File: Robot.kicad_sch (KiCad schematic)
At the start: 5 parts, among them J1 XT60 4Port PDB, J2 LM2596 Buck Converter, J3 WAGO 221 - 5 Port

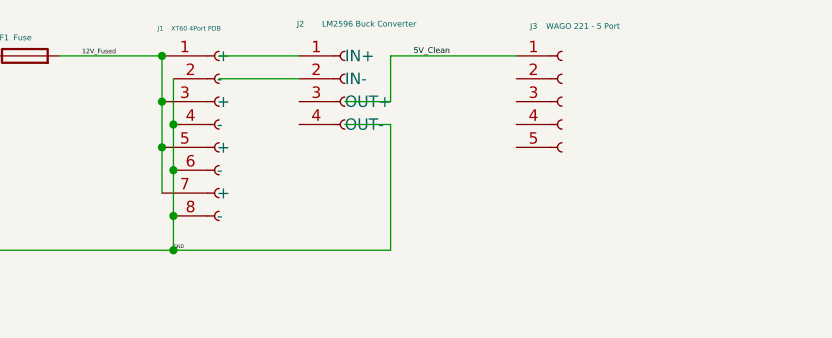
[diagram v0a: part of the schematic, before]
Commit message: fix some stupid mistakes; connect wires to devices from WAGO 221; add PWR_FLAG
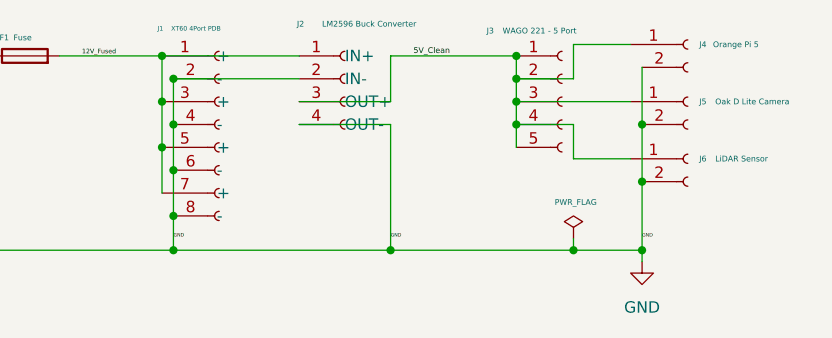
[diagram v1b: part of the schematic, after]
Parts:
- added J4: Orange Pi 5, symbol Connector:Conn_01x02_Socket
- added J5: Oak D Lite Camera, symbol Connector:Conn_01x02_Socket
- added J6: LiDAR Sensor, symbol Connector:Conn_01x02_Socket
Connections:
- net 12V_Fused: now also J2.1 (IN+)
- net 5V_Clean: now also J2.3 (OUT+), J3.2 (Pin_2), J3.3 (Pin_3), J3.4 (Pin_4), J3.5 (Pin_5), J4.1 (Pin_1), J5.1 (Pin_1), J6.1 (Pin_1)
- net GND: now also J2.2 (IN-), J2.4 (OUT-), J4.2 (Pin_2), J5.2 (Pin_2), J6.2 (Pin_2)

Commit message: add name for sheet; add more power flags for 12V_Fused and 5V_Clean
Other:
- title: (none) -> AI Robot Schematic
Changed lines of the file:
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@@
 	(generator_version "10.0")
 	(paper "A4")
+	(title_block
+		(title "AI Robot Schematic")
+		(date "2026-07-07")
+		(rev "0")
+	)
+	(junction
+		(at 62.23 80.01)
+		(diameter 0)
+		(color 0 0 0 0)
+	)
 	(junction
 		(at 104.14 80.01)
@@
 	)
 	(junction
+		(at 99.06 80.01)
+		(diameter 0)
+		(color 0 0 0 0)
+	)
+	(junction
 		(at 66.04 82.55)
 		(diameter 0)
@@
 	(wire
 		(pts
-			(xy 53.34 80.01) (xy 64.77 80.01)
+			(xy 53.34 80.01) (xy 62.23 80.01)
+		)
+		(stroke
+			(width 0)
+			(type default)
+		)
+	)
+	(wire
+		(pts
+			(xy 99.06 78.74) (xy 99.06 80.01)
+		)
+		(stroke
+			(width 0)
+			(type default)
+		)
+	)
+	(wire
+		(pts
+			(xy 62.23 78.74) (xy 62.23 80.01)
 		)
 		(stroke
@@
 	(wire
 		(pts
+			(xy 99.06 80.01) (xy 104.14 80.01)
+		)
+		(stroke
+			(width 0)
+			(type default)
+		)
+	)
+	(wire
+		(pts
 			(xy 66.04 101.6) (xy 90.17 101.6)
 		)
@@
 	(wire
 		(pts
-			(xy 90.17 80.01) (xy 104.14 80.01)
+			(xy 90.17 80.01) (xy 99.06 80.01)
 		)
 		(stroke
@@
 		(pts
 			(xy 64.77 80.01) (xy 64.77 85.09)
+		)
+		(stroke
+			(width 0)
+			(type default)
+		)
+	)
+	(wire
+		(pts
+			(xy 62.23 80.01) (xy 64.77 80.01)
 		)
 		(stroke
@@
 	)
 	(symbol
+		(lib_id "power:PWR_FLAG")
+		(at 62.23 78.74 0)
+		(unit 1)
+		(body_style 1)
+		(exclude_from_sim no)
+		(in_bom yes)
+		(on_board yes)
+		(in_pos_files yes)
+		(dnp no)
+		(property "Reference" "#FLG05"
+			(at 62.23 76.835 0)
+			(hide yes)
+			(show_name no)
+			(do_not_autoplace no)
+			(effects
+				(font
+					(size 1.27 1.27)
+				)
+			)
+		)
+		(property "Value" "PWR_FLAG"
+			(at 62.484 74.676 0)
+			(show_name no)
+			(do_not_autoplace no)
+			(effects
+				(font
+					(size 0.635 0.635)
+				)
+			)
+		)
+		(property "Footprint" ""
+			(at 62.23 78.74 0)
+			(hide yes)
+			(show_name no)
+			(do_not_autoplace no)
+			(effects
+				(font
+					(size 1.27 1.27)
+				)
+			)
+		)
+		(property "Datasheet" ""
+			(at 62.23 78.74 0)
+			(hide yes)
+			(show_name no)
+			(do_not_autoplace no)
+			(effects
+				(font
+					(size 1.27 1.27)
+				)
+			)
+		)
+		(property "Description" "Special symbol for telling ERC where power comes from"
+			(at 62.23 78.74 0)
+			(hide yes)
+			(show_name no)
+			(do_not_autoplace no)
+			(effects
+				(font
+					(size 1.27 1.27)
+				)
+			)
+		)
+		(pin "1"
+		)
+		(instances
+			(project "Robot"
+				(path "/5327e841-c188-4aaa-a450-fde1e5fc6222"
+					(reference "#FLG05")
+					(unit 1)
+				)
+			)
+		)
+	)
+	(symbol
 		(lib_id "power:GND")
 		(at 118.11 102.87 0)
@@
 					(unit 1)
 				)
+			)
+		)
+	)
+	(symbol
+		(lib_id "power:PWR_FLAG")
+		(at 99.06 78.74 0)
+		(unit 1)
+		(body_style 1)
+		(exclude_from_sim no)
+		(in_bom yes)
+		(on_board yes)
+		(in_pos_files yes)
+		(dnp no)
+		(property "Reference" "#FLG06"
+			(at 99.06 76.835 0)
+			(hide yes)
+			(show_name no)
+			(do_not_autoplace no)
+			(effects
+				(font
+					(size 1.27 1.27)
+				)
+			)
+		)
+		(property "Value" "PWR_FLAG"
+			(at 99.314 74.676 0)
+			(show_name no)
+			(do_not_autoplace no)
+			(effects
+				(font
+					(size 0.635 0.635)
+				)
+			)
+		)
+		(property "Footprint" ""
+			(at 99.06 78.74 0)
+			(hide yes)
+			(show_name no)
+			(do_not_autoplace no)
+			(effects
+				(font
+					(size 1.27 1.27)
+				)
+			)
+		)
+		(property "Datasheet" ""
+			(at 99.06 78.74 0)
+			(hide yes)
+			(show_name no)
+			(do_not_autoplace no)
+			(effects
+				(font
+					(size 1.27 1.27)
+				)
+			)
+		)
+		(property "Description" "Special symbol for telling ERC where power comes from"
+			(at 99.06 78.74 0)
+			(hide yes)
+			(show_name no)
+			(do_not_autoplace no)
+			(effects
+				(font
+					(size 1.27 1.27)
+				)
+			)
+		)
+		(pin "1"
+		)
+		(instances
+			(project "Robot"
+				(path "/5327e841-c188-4aaa-a450-fde1e5fc6222"
+					(reference "#FLG06")
+					(unit 1)
+				)

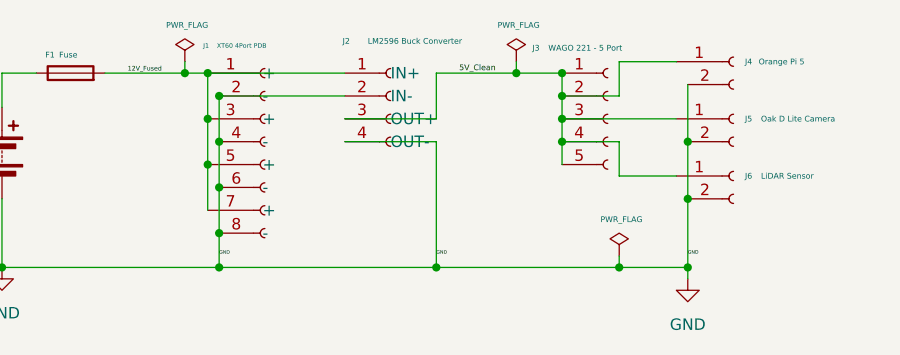
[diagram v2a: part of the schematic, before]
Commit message: add elegoo mega 2560 to wago 221
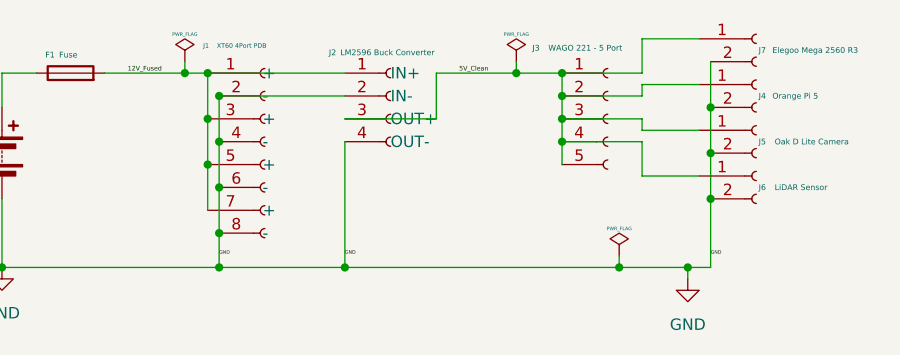
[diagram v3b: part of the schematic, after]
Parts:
- added J7: Elegoo Mega 2560 R3, symbol Connector:Conn_01x02_Socket
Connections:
- net 5V_Clean: now also J7.1 (Pin_1)
- net GND: now also J7.2 (Pin_2)
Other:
- moved on the sheet: J4, J5, J6

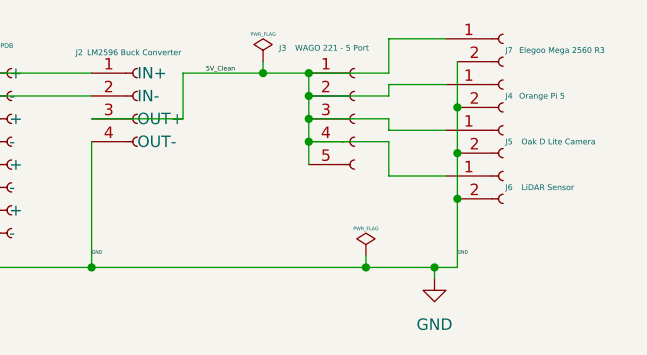
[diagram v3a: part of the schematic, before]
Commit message: remove message under pin 5 of WAGO; move bottom right gnd wire; wire elegoo mega 2560 r3 to port 1 of WAGO
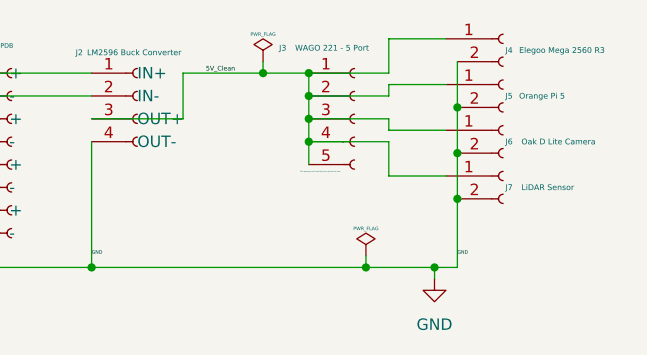
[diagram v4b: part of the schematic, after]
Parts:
- renumbered J7 to J4, J4 to J5, J5 to J6, J6 to J7
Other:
- note added: "This extra port will most likely be used for the claw"
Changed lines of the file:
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@@
 		(rev "0")
+	)
+	(text "This extra port will most likely be used for the claw"
+		(exclude_from_sim no)
+		(at 105.41 91.186 0)
+		(effects
+			(font
+				(size 0.127 0.127)
+			)
+		)
 	)
 	(junction
@@
 		(in_pos_files yes)
 		(dnp no)
-		(property "Reference" "J6"
+		(property "Reference" "J7"
 			(at 125.984 92.71 0)
 			(show_name no)
@@
 			(project "Robot"
 				(path "/5327e841-c188-4aaa-a450-fde1e5fc6222"
-					(reference "J6")
+					(reference "J7")
 					(unit 1)
 				)
@@
 		(in_pos_files yes)
 		(dnp no)
-		(property "Reference" "J5"
+		(property "Reference" "J6"
 			(at 125.984 87.63 0)
 			(show_name no)
@@
 			(project "Robot"
 				(path "/5327e841-c188-4aaa-a450-fde1e5fc6222"
-					(reference "J5")
+					(reference "J6")
 					(unit 1)
 				)
@@
 		(in_pos_files yes)
 		(dnp no)
-		(property "Reference" "J4"
+		(property "Reference" "J5"
 			(at 125.984 82.55 0)
 			(show_name no)
@@
 			(project "Robot"
 				(path "/5327e841-c188-4aaa-a450-fde1e5fc6222"
-					(reference "J4")
+					(reference "J5")
 					(unit 1)
 				)
@@
 		(in_pos_files yes)
 		(dnp no)
-		(property "Reference" "J7"
+		(property "Reference" "J4"
 			(at 125.984 77.47 0)
 			(show_name no)
@@
 			(project "Robot"
 				(path "/5327e841-c188-4aaa-a450-fde1e5fc6222"
-					(reference "J7")
+					(reference "J4")
 					(unit 1)
 				)

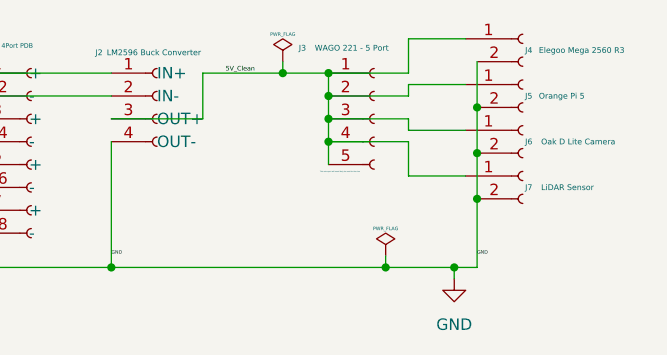
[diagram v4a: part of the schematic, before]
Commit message: remove message under pin 5 of WAGO; move bottom right gnd wire; wire elegoo mega 2560 r3 to port 1 of WAGO. This is the same message from previous commit, because I forgot to save the sch file
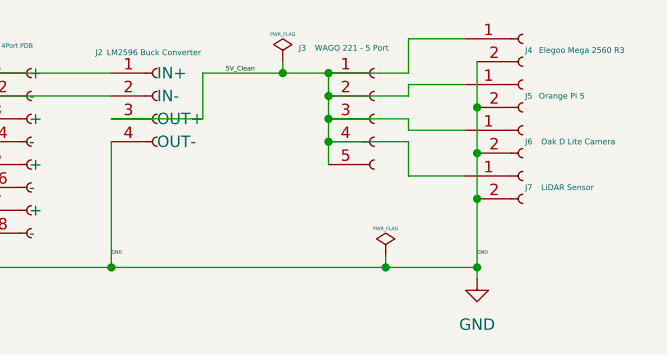
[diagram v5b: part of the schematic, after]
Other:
- note removed: "This extra port will most likely be used for the claw"
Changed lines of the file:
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@@
 		(rev "0")
 	)
-	(text "This extra port will most likely be used for the claw"
-		(exclude_from_sim no)
-		(at 105.41 91.186 0)
-		(effects
-			(font
-				(size 0.127 0.127)
-			)
-		)
+	(junction
+		(at 120.65 101.6)
+		(diameter 0)
+		(color 0 0 0 0)
 	)
 	(junction
@@
 	)
 	(junction
-		(at 118.11 101.6)
-		(diameter 0)
-		(color 0 0 0 0)
-	)
-	(junction
 		(at 41.91 101.6)
 		(diameter 0)
@@
 	(wire
 		(pts
-			(xy 118.11 101.6) (xy 118.11 102.87)
-		)
-		(stroke
-			(width 0)
-			(type default)
-		)
-	)
-	(wire
-		(pts
 			(xy 113.03 76.2) (xy 119.38 76.2)
 		)
@@
 	(wire
 		(pts
+			(xy 120.65 101.6) (xy 120.65 102.87)
+		)
+		(stroke
+			(width 0)
+			(type default)
+		)
+	)
+	(wire
+		(pts
 			(xy 64.77 80.01) (xy 80.01 80.01)
 		)
@@
 	(wire
 		(pts
-			(xy 110.49 101.6) (xy 118.11 101.6)
+			(xy 110.49 101.6) (xy 120.65 101.6)
 		)
 		(stroke
@@
 		(pts
 			(xy 90.17 80.01) (xy 99.06 80.01)
-		)
-		(stroke
-			(width 0)
-			(type default)
-		)
-	)
-	(wire
-		(pts
-			(xy 120.65 101.6) (xy 118.11 101.6)
 		)
 		(stroke
@@
 	)
 	(symbol
+		(lib_id "power:GND")
+		(at 120.65 102.87 0)
+		(unit 1)
+		(body_style 1)
+		(exclude_from_sim no)
+		(in_bom yes)
+		(on_board yes)
+		(in_pos_files yes)
+		(dnp no)
+		(fields_autoplaced yes)
+		(property "Reference" "#PWR02"
+			(at 120.65 109.22 0)
+			(hide yes)
+			(show_name no)
+			(do_not_autoplace no)
+			(effects
+				(font
+					(size 1.27 1.27)
+				)
+			)
+		)
+		(property "Value" "GND"
+			(at 120.65 107.95 0)
+			(show_name no)
+			(do_not_autoplace no)
+			(effects
+				(font
+					(size 1.27 1.27)
+				)
+			)
+		)
+		(property "Footprint" ""
+			(at 120.65 102.87 0)
+			(hide yes)
+			(show_name no)
+			(do_not_autoplace no)
+			(effects
+				(font
+					(size 1.27 1.27)
+				)
+			)
+		)
+		(property "Datasheet" ""
+			(at 120.65 102.87 0)
+			(hide yes)
+			(show_name no)
+			(do_not_autoplace no)
+			(effects
+				(font
+					(size 1.27 1.27)
+				)
+			)
+		)
+		(property "Description" "Power symbol creates a global label with name \"GND\" , ground"
+			(at 120.65 102.87 0)
+			(hide yes)
+			(show_name no)
+			(do_not_autoplace no)
+			(effects
+				(font
+					(size 1.27 1.27)
+				)
+			)
+		)
+		(pin "1"
+		)
+		(instances
+			(project "Robot"
+				(path "/5327e841-c188-4aaa-a450-fde1e5fc6222"
+					(reference "#PWR02")
+					(unit 1)
+				)
+			)
+		)
+	)
+	(symbol
 		(lib_id "Connector:Conn_01x08_Socket")
 		(at 71.12 87.63 0)
@@
 					(unit 1)
 				)
-			)
-		)
-	)
-	(symbol
-		(lib_id "power:GND")
-		(at 118.11 102.87 0)
-		(unit 1)
-		(body_style 1)
-		(exclude_from_sim no)
-		(in_bom yes)
-		(on_board yes)
-		(in_pos_files yes)
-		(dnp no)
-		(fields_autoplaced yes)
-		(property "Reference" "#PWR02"
-			(at 118.11 109.22 0)
-			(hide yes)
-			(show_name no)
-			(do_not_autoplace no)
-			(effects
-				(font
-					(size 1.27 1.27)
-				)
-			)
-		)
-		(property "Value" "GND"
-			(at 118.11 107.95 0)
-			(show_name no)
-			(do_not_autoplace no)
-			(effects
-				(font
-					(size 1.27 1.27)
-				)
-			)
-		)
-		(property "Footprint" ""
-			(at 118.11 102.87 0)
-			(hide yes)
-			(show_name no)
-			(do_not_autoplace no)
-			(effects
-				(font
-					(size 1.27 1.27)
-				)
-			)
-		)
-		(property "Datasheet" ""
-			(at 118.11 102.87 0)
-			(hide yes)
-			(show_name no)
-			(do_not_autoplace no)
-			(effects
-				(font
-					(size 1.27 1.27)
-				)
-			)
-		)
-		(property "Description" "Power symbol creates a global label with name \"GND\" , ground"
-			(at 118.11 102.87 0)
-			(hide yes)
-			(show_name no)
-			(do_not_autoplace no)
-			(effects
-				(font
-					(size 1.27 1.27)
-				)
-			)
-		)
-		(pin "1"
-		)
-		(instances
-			(project "Robot"
-				(path "/5327e841-c188-4aaa-a450-fde1e5fc6222"
-					(reference "#PWR02")
-					(unit 1)
-				)

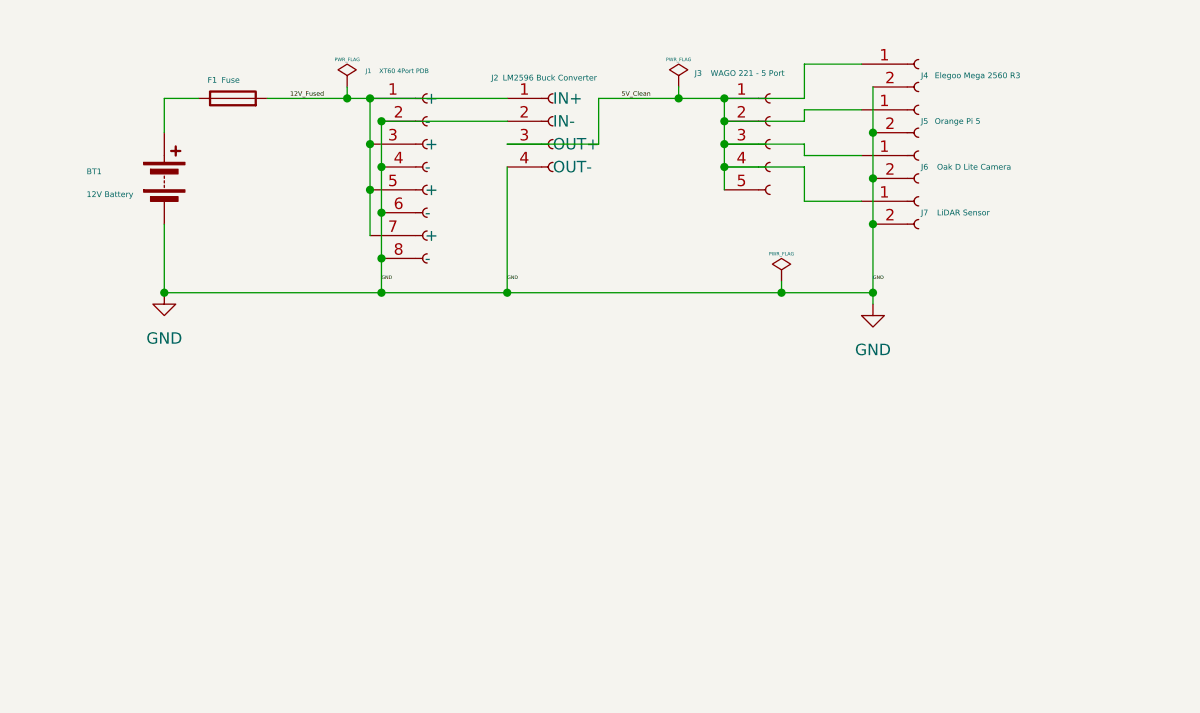
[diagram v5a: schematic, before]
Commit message: add 2 Cytron MDD10A motor drivers into schematic
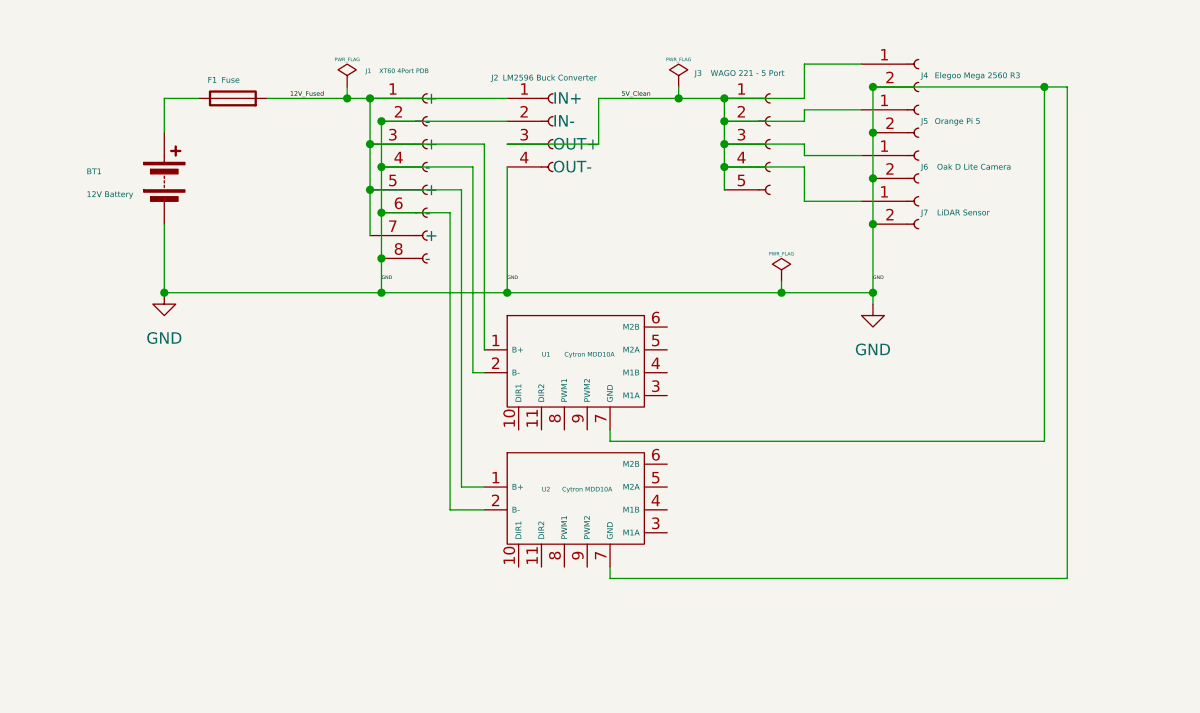
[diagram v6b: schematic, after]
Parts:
- added U1, U2: Cytron MDD10A, symbol Custom_Components:Cytron_MDD10A
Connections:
- net 12V_Fused: now also U1.1 (B+), U2.1 (B+)
- net GND: now also U1.2 (B-), U1.7 (GND), U2.2 (B-), U2.7 (GND)

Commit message: replace f1 fuse with circuit breaker; add a 5A inline fuse between pin 1 of J1 and J2; add 20A fuses on motor driver B+ pins
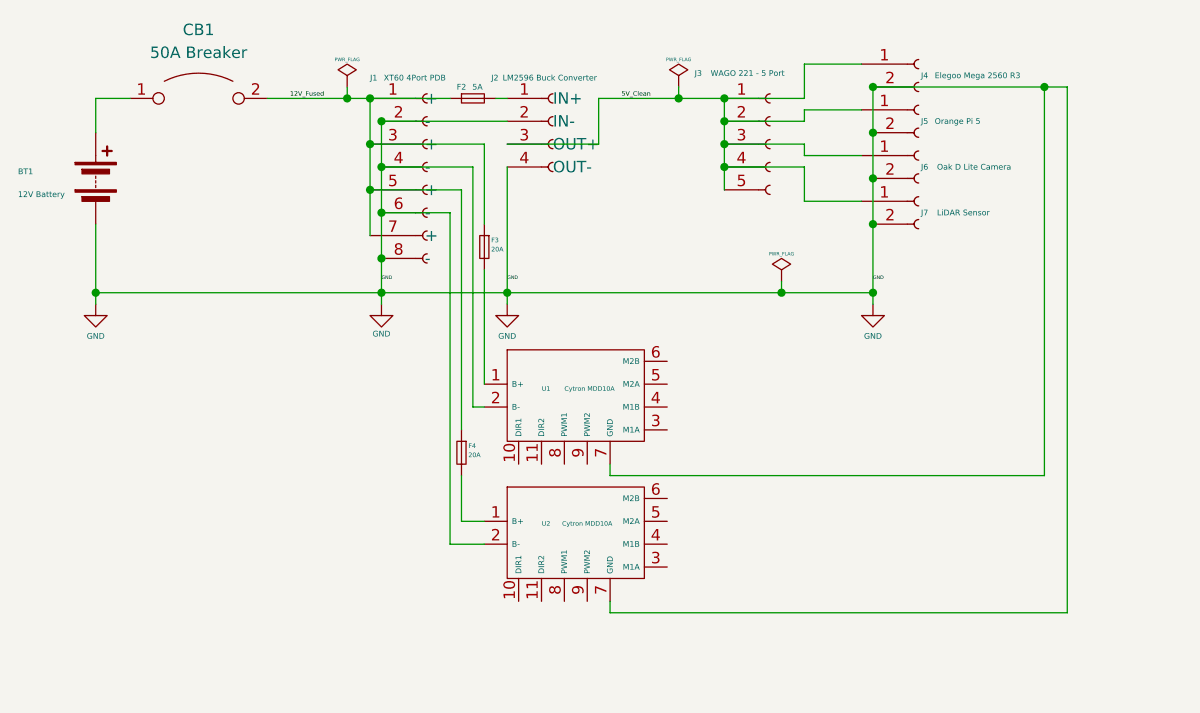
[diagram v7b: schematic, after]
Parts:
- removed F1: Fuse, symbol Device:Fuse
- added CB1: 50A Breaker, symbol Device:CircuitBreaker_1P_US
- added F2: 5A, symbol Device:Fuse_Small
- added F3, F4: 20A, symbol Device:Fuse_Small
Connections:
- net 12V_Fused: now also CB1.2, F2.1, F3.1, F4.1; no longer J2.1 (IN+), U1.1 (B+), U2.1 (B+)
- net at BT1.1 (+): now also CB1.1
- new net: F2.2, J2.1 (IN+)
- new net: F4.2, U2.1 (B+)
- new net: F3.2, U1.1 (B+)
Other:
- moved on the sheet: BT1, U1, U2

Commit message: edit
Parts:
- removed J2: LM2596 Buck Converter, symbol Connector:Conn_01x04_Socket
- removed J4: Elegoo Mega 2560 R3, symbol Connector:Conn_01x02_Socket
- added F1: 1A, symbol Device:Fuse_Small
- added J2, J4: LM2596 Buck Converter, symbol Custom_Components:LM2596_Buck_Converter
- added U3, U5: JGB37-520, symbol Custom_Components:JGB37-520_12V
- CB1: value 50A Breaker -> 10A Breaker
- F3, F4: value 20A -> 3A
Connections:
- net 12V_Fused: now also J4.1 (IN+); no longer F3.1, F4.1
- net 5V_Clean: now also J2.3 (OUT+)
- net GND: now also J2.2 (IN-), J2.4 (OUT-), J4.2 (IN-), J4.4 (OUT-); no longer U1.2 (B-), U1.7 (GND), U2.2 (B-), U2.7 (GND)
- net at F2.2: now also J2.1 (IN+)
- net at F4.2: no longer U2.1 (B+)
- net at U1.1 (B+): no longer F3.2
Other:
- moved on the sheet: F3, F4, J3, J5, J6, J7
